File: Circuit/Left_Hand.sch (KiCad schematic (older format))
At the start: 8 parts, among them P1 Wall, P2 CW, P3 Enable, P4 CCW

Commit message: 実態配線図書き始め
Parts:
- P1, P2, P3, P4: footprint (none) -> YASU:XA_2Pin
- R5, R6, R7, R8: footprint (none) -> Resistors_SMD:R_0603_HandSoldering
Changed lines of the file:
@@
 LIBS:contrib
 LIBS:valves
+LIBS:YASU
 LIBS:device
+LIBS:robocon_sch
 LIBS:rhand_controller-cache
 EELAYER 25 0
@@
 F 0 "P2" H 3800 3750 50  0000 C CNN
 F 1 "CW" V 3900 3600 50  0000 C CNN
-F 2 "" H 3800 3600 50  0000 C CNN
+F 2 "YASU:XA_2Pin" H 3800 3600 50  0001 C CNN
 F 3 "" H 3800 3600 50  0000 C CNN
 	1    3800 3600
@@
 F 0 "R6" V 4130 3300 50  0000 C CNN
 F 1 "10k" V 4050 3300 50  0000 C CNN
-F 2 "" V 3980 3300 50  0000 C CNN
+F 2 "Resistors_SMD:R_0603_HandSoldering" V 3980 3300 50  0001 C CNN
 F 3 "" H 4050 3300 50  0000 C CNN
 	1    4050 3300
@@
 F 0 "P4" H 4650 3750 50  0000 C CNN
 F 1 "CCW" V 4750 3600 50  0000 C CNN
-F 2 "" H 4650 3600 50  0000 C CNN
+F 2 "YASU:XA_2Pin" H 4650 3600 50  0001 C CNN
 F 3 "" H 4650 3600 50  0000 C CNN
 	1    4650 3600
@@
 F 0 "R8" V 4980 3300 50  0000 C CNN
 F 1 "10k" V 4900 3300 50  0000 C CNN
-F 2 "" V 4830 3300 50  0000 C CNN
+F 2 "Resistors_SMD:R_0603_HandSoldering" V 4830 3300 50  0001 C CNN
 F 3 "" H 4900 3300 50  0000 C CNN
 	1    4900 3300
@@
 F 0 "P1" H 3700 5300 50  0000 C CNN
 F 1 "Wall" V 3800 5150 50  0000 C CNN
-F 2 "" H 3700 5150 50  0000 C CNN
+F 2 "YASU:XA_2Pin" H 3700 5150 50  0001 C CNN
 F 3 "" H 3700 5150 50  0000 C CNN
 	1    3700 5150
@@
 F 0 "R5" V 4030 4850 50  0000 C CNN
 F 1 "10k" V 3950 4850 50  0000 C CNN
-F 2 "" V 3880 4850 50  0000 C CNN
+F 2 "Resistors_SMD:R_0603_HandSoldering" V 3880 4850 50  0001 C CNN
 F 3 "" H 3950 4850 50  0000 C CNN
 	1    3950 4850
@@
 F 0 "P3" H 4600 5300 50  0000 C CNN
 F 1 "Enable" V 4700 5150 50  0000 C CNN
-F 2 "" H 4600 5150 50  0000 C CNN
+F 2 "YASU:XA_2Pin" H 4600 5150 50  0001 C CNN
 F 3 "" H 4600 5150 50  0000 C CNN
 	1    4600 5150
@@
 F 0 "R7" V 4930 4850 50  0000 C CNN
 F 1 "10k" V 4850 4850 50  0000 C CNN
-F 2 "" V 4780 4850 50  0000 C CNN
+F 2 "Resistors_SMD:R_0603_HandSoldering" V 4780 4850 50  0001 C CNN
 F 3 "" H 4850 4850 50  0000 C CNN
 	1    4850 4850

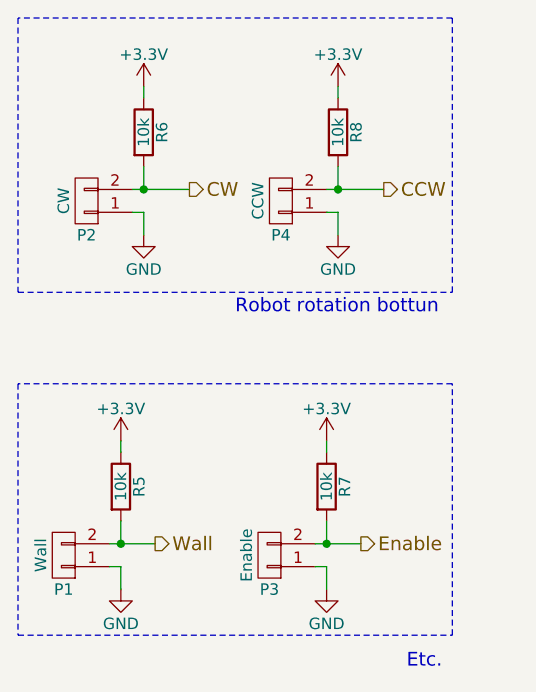
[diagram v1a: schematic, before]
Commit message: 部品割り付けの完了
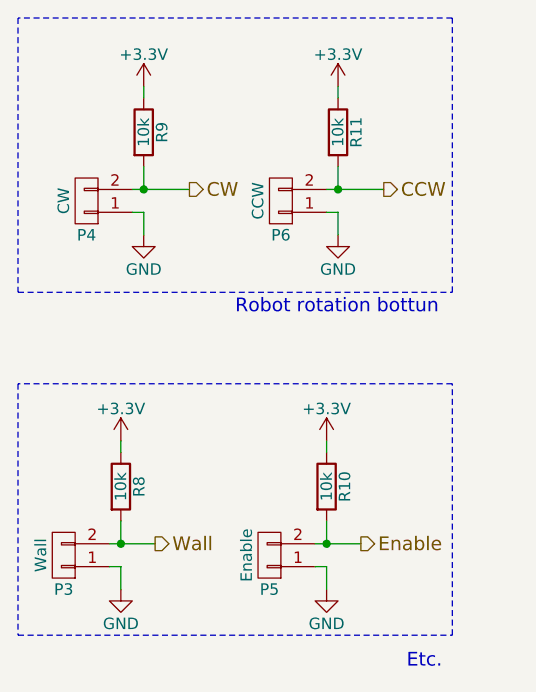
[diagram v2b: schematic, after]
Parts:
- renumbered P1 to P3, P2 to P4, P3 to P5, P4 to P6, R7 to R10, R8 to R11, R5 to R8, R6 to R9
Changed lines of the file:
@@
 LIBS:YASU
 LIBS:device
-LIBS:robocon_sch
 LIBS:rhand_controller-cache
 EELAYER 25 0
@@
 $EndDescr
 $Comp
-L CONN_01X02 P2
+L CONN_01X02 P4
 U 1 1 593BE59D
 P 3800 3600
-F 0 "P2" H 3800 3750 50  0000 C CNN
+F 0 "P4" H 3800 3750 50  0000 C CNN
 F 1 "CW" V 3900 3600 50  0000 C CNN
 F 2 "YASU:XA_2Pin" H 3800 3600 50  0001 C CNN
@@
 $EndComp
 $Comp
-L R R6
+L R R9
 U 1 1 593BE5AF
 P 4050 3300
-F 0 "R6" V 4130 3300 50  0000 C CNN
+F 0 "R9" V 4130 3300 50  0000 C CNN
 F 1 "10k" V 4050 3300 50  0000 C CNN
 F 2 "Resistors_SMD:R_0603_HandSoldering" V 3980 3300 50  0001 C CNN
@@
 $EndComp
 $Comp
-L CONN_01X02 P4
+L CONN_01X02 P6
 U 1 1 593BE5BE
 P 4650 3600
-F 0 "P4" H 4650 3750 50  0000 C CNN
+F 0 "P6" H 4650 3750 50  0000 C CNN
 F 1 "CCW" V 4750 3600 50  0000 C CNN
 F 2 "YASU:XA_2Pin" H 4650 3600 50  0001 C CNN
@@
 $EndComp
 $Comp
-L R R8
+L R R11
 U 1 1 593BE5D0
 P 4900 3300
-F 0 "R8" V 4980 3300 50  0000 C CNN
+F 0 "R11" V 4980 3300 50  0000 C CNN
 F 1 "10k" V 4900 3300 50  0000 C CNN
 F 2 "Resistors_SMD:R_0603_HandSoldering" V 4830 3300 50  0001 C CNN
@@
 $EndComp
 $Comp
-L CONN_01X02 P1
+L CONN_01X02 P3
 U 1 1 593BE5DF
 P 3700 5150
-F 0 "P1" H 3700 5300 50  0000 C CNN
+F 0 "P3" H 3700 5300 50  0000 C CNN
 F 1 "Wall" V 3800 5150 50  0000 C CNN
 F 2 "YASU:XA_2Pin" H 3700 5150 50  0001 C CNN
@@
 $EndComp
 $Comp
-L R R5
+L R R8
 U 1 1 593BE5F1
 P 3950 4850
-F 0 "R5" V 4030 4850 50  0000 C CNN
+F 0 "R8" V 4030 4850 50  0000 C CNN
 F 1 "10k" V 3950 4850 50  0000 C CNN
 F 2 "Resistors_SMD:R_0603_HandSoldering" V 3880 4850 50  0001 C CNN
@@
 $EndComp
 $Comp
-L CONN_01X02 P3
+L CONN_01X02 P5
 U 1 1 593BE601
 P 4600 5150
-F 0 "P3" H 4600 5300 50  0000 C CNN
+F 0 "P5" H 4600 5300 50  0000 C CNN
 F 1 "Enable" V 4700 5150 50  0000 C CNN
 F 2 "YASU:XA_2Pin" H 4600 5150 50  0001 C CNN
@@
 $EndComp
 $Comp
-L R R7
+L R R10
 U 1 1 593BE613
 P 4850 4850
-F 0 "R7" V 4930 4850 50  0000 C CNN
+F 0 "R10" V 4930 4850 50  0000 C CNN
 F 1 "10k" V 4850 4850 50  0000 C CNN
 F 2 "Resistors_SMD:R_0603_HandSoldering" V 4780 4850 50  0001 C CNN

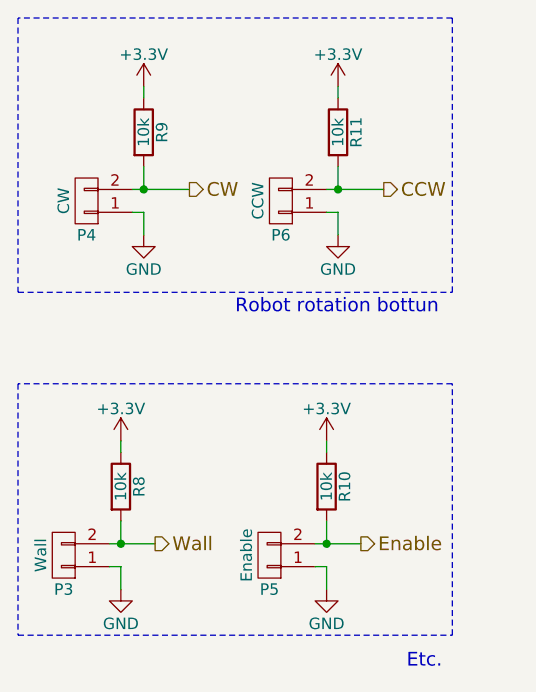
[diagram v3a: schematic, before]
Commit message: ADCのピン配置修正と配線引きはじめ
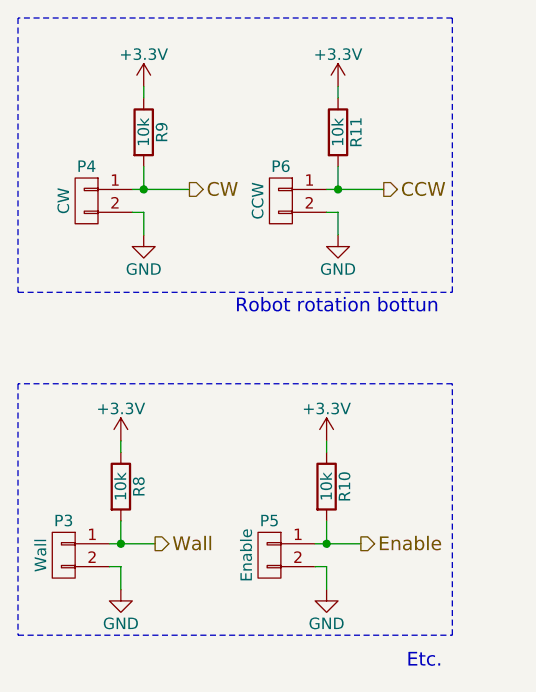
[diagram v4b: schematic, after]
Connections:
- net CCW: now also P6.1 (P1); no longer P6.2 (P2)
- net CW: now also P4.1 (P1); no longer P4.2 (P2)
- net Enable: now also P5.1 (P1); no longer P5.2 (P2)
- net GND: now also P3.2 (P2), P4.2 (P2), P5.2 (P2), P6.2 (P2); no longer P3.1 (P1), P4.1 (P1), P5.1 (P1), P6.1 (P1)
- net Wall: now also P3.1 (P1); no longer P3.2 (P2)
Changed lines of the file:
@@
 LIBS:contrib
 LIBS:valves
-LIBS:YASU
 LIBS:device
+LIBS:robocon_sch
 LIBS:rhand_controller-cache
 EELAYER 25 0
@@
 F 3 "" H 3800 3600 50  0000 C CNN
 	1    3800 3600
-	-1   0    0    1
+	-1   0    0    -1
 $EndComp
 Wire Wire Line
@@
 F 3 "" H 4650 3600 50  0000 C CNN
 	1    4650 3600
-	-1   0    0    1
+	-1   0    0    -1
 $EndComp
 Wire Wire Line
@@
 F 3 "" H 3700 5150 50  0000 C CNN
 	1    3700 5150
-	-1   0    0    1
+	-1   0    0    -1
 $EndComp
 Wire Wire Line
@@
 F 3 "" H 4600 5150 50  0000 C CNN
 	1    4600 5150
-	-1   0    0    1
+	-1   0    0    -1
 $EndComp
 Wire Wire Line

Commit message: あらかた終わったぞ
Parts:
- R10, R11, R8, R9: footprint Resistors_SMD:R_0603_HandSoldering -> Resistors_ThroughHole:R_Axial_DIN0207_L6.3mm_D2.5mm_P7.62mm_Horizontal
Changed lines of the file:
@@
 F 0 "R9" V 4130 3300 50  0000 C CNN
 F 1 "10k" V 4050 3300 50  0000 C CNN
-F 2 "Resistors_SMD:R_0603_HandSoldering" V 3980 3300 50  0001 C CNN
+F 2 "Resistors_ThroughHole:R_Axial_DIN0207_L6.3mm_D2.5mm_P7.62mm_Horizontal" V 3980 3300 50  0001 C CNN
 F 3 "" H 4050 3300 50  0000 C CNN
 	1    4050 3300
@@
 F 0 "R11" V 4980 3300 50  0000 C CNN
 F 1 "10k" V 4900 3300 50  0000 C CNN
-F 2 "Resistors_SMD:R_0603_HandSoldering" V 4830 3300 50  0001 C CNN
+F 2 "Resistors_ThroughHole:R_Axial_DIN0207_L6.3mm_D2.5mm_P7.62mm_Horizontal" V 4830 3300 50  0001 C CNN
 F 3 "" H 4900 3300 50  0000 C CNN
 	1    4900 3300
@@
 F 0 "R8" V 4030 4850 50  0000 C CNN
 F 1 "10k" V 3950 4850 50  0000 C CNN
-F 2 "Resistors_SMD:R_0603_HandSoldering" V 3880 4850 50  0001 C CNN
+F 2 "Resistors_ThroughHole:R_Axial_DIN0207_L6.3mm_D2.5mm_P7.62mm_Horizontal" V 3880 4850 50  0001 C CNN
 F 3 "" H 3950 4850 50  0000 C CNN
 	1    3950 4850
@@
 F 0 "R10" V 4930 4850 50  0000 C CNN
 F 1 "10k" V 4850 4850 50  0000 C CNN
-F 2 "Resistors_SMD:R_0603_HandSoldering" V 4780 4850 50  0001 C CNN
+F 2 "Resistors_ThroughHole:R_Axial_DIN0207_L6.3mm_D2.5mm_P7.62mm_Horizontal" V 4780 4850 50  0001 C CNN
 F 3 "" H 4850 4850 50  0000 C CNN
 	1    4850 4850
